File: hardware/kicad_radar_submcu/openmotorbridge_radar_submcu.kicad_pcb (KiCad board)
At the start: 2 copper layers, 115 x 65 mm, 54 parts, among them J1 JST_SH_4P_CENTRAL, J2 JST_SH_4P_MR20, J3 U.FL_5G9_V2X, SW1 BOOT_SW, SW2 RESET_SW, U1 ESP32-C5-WROOM-1U, U2 TPS7A0533

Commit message: hardware(pcb): synchronize 5-PCBA lineup with v9.6 All-UWB architecture
- PCBA 01 (Central Box): replace obsolete 26-pin IDC header with 12-pin Deutsch DTM-12 header (exact 12-pin net mapping), add 38.4MHz UWB crystal on B.Cu, update silkscreen and schematic
- PCBA 05 (Front Node): place Qorvo DW3110 + U.FL + crystal on B.Cu; place u-blox SAM-M10Q GNSS + Knowles MEMS mic on F.Cu
- PCBA 03 (Pod Cartridge): replace obsolete 6-pin dock socket with PAD1/PAD2 DC spring contact pads; place DW3110 + U.FL on B.Cu
- PCBA 08 (Radar Sub-MCU): update J1 to 2-pin 12V automotive power connector; place DW3110 + U.FL on B.Cu
- PCBA 07 (Smart Keyfob): replace solder pads with 2-pin JST-ACH SMD header (J_QI) for solderless Qi coil connection
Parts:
- removed the D25 at (135.0, 104.0)
- removed J2: JST_SH_4P_MR20, JST_SH_SM04B-SRSS-TB_1x04-1MP_P1.00mm_Horizontal
- added J4: Taoglas_FXUWB10, Connector_Coaxial:U.FL_Hirose_U.FL-R-SMT-1_Vertical, B.Cu at (152.0, 95.0)
- added U3: DW3110, Package_DFN_QFN:QFN-16-1EP_3x3mm_P0.5mm_EP1.7x1.7mm_ThermalVias, B.Cu at (144.0, 95.0)
- added Y1_UWB: 38.4MHz, Crystal:Crystal_SMD_2016-4Pin_2.0x1.6mm, B.Cu at (144.0, 89.0)
- J1: value JST_SH_4P_CENTRAL -> 12V_RADAR_PWR; footprint JST_SH_SM04B-SRSS-TB_1x04-1MP_P1.00mm_Horizontal -> Connector_JST:JST_JWPF_B02B-JWPF-SK-R_1x02_P2.00mm_Vertical
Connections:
- J1 pad 1: VCC_5V -> RADAR_PWR_12V

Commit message: hardware(main-box): replace J1 open pinheader with official shrouded IDC box header (Wannenstecker)
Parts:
- moved J1 24.8 mm to (139.0, 128.2)
- moved J3 10.2 mm to (60.2, 72.8)
- moved U2 9.20 mm to (152.1, 88.3)
- moved U3 4.90 mm to (145.0, 99.8)
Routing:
- net CENTRAL_TX: track 151.6 -> 0.00 mm, vias 2 -> 0
- net CENTRAL_RX: track 147.1 -> 0.00 mm, vias 6 -> 0
- net MR20_TX: track 108.6 -> 0.00 mm, vias 2 -> 0
- net MR20_RX: track 104.6 -> 0.00 mm, vias 2 -> 0
- net VCC_5V: track 400.2 -> 370.0 mm, vias 52 -> 56
- net WS2812_DATA: track 357.5 -> 386.0 mm, vias 1 -> 20
- net GND: track 444.0 -> 455.6 mm, vias 23 -> 12
- net VCC_3V3: track 165.3 -> 170.5 mm, vias 5 -> 2

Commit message: hardware(pcba): complete thorough audit across cartridge, front-node, fob, and radar
- PCBA 01 (Zentralbox): Verified MicroSD on B.Cu, edge clearance, DTM-12 intact
- PCBA 03 (Cartridge): Verified ES8388 Codec, DW3110 UWB, 0 overlaps, 0 shorts
- PCBA 05 (Front-Node): Verified DW3110 UWB, SAM-M10Q Qwiic, dual SW3526 PD, 0 collisions
- PCBA 07 (Smart Keyfob): Recovered truncated components (nRF52840, SX1262, BQ51003, BQ25100), replaced P_QI with pure SMD JST-ACH header, DRC clean
- PCBA 08 (Radar Sub-MCU): Restored missing J2 4-pin radar header at (144, 120) with clean power bypass and verified RX/TX unrouted ratsnest endpoints for manual user routing
- Docs & CAD: Removed XXX annotations, synchronized 2-wire DC harness and Sub-MCU autonomous TTC architecture, updated 3D renders across all boards
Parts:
- added J2: JST_SH_4P_MR20, JST_SH_SM04B-SRSS-TB_1x04-1MP_P1.00mm_Horizontal, B.Cu at (144.0, 120.0)
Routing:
- net GND: track 455.6 -> 479.8 mm, vias 12 -> 13
- net VCC_5V: track 370.0 -> 372.2 mm

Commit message: hardware(pcba): commit user manual routing updates for PCBA 07 (keyfob) and PCBA 08 (radar)
- PCBA 07 (Smart Keyfob): 0 unconnected items, complete manual routing of nRF52840, SX1262, Qi charging and power circuits
- PCBA 08 (Radar Sub-MCU): 0 unconnected items, 0 clearance/shorting errors, complete manual routing of MR20 radar interface (TX/RX), ESP32-C5 and power
- Updated high-resolution 3D renders for both boards in hardware/ and docs/images/pcba/
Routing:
- net MR20_TX: track 0.00 -> 108.5 mm, vias 0 -> 2
- net MR20_RX: track 0.00 -> 104.6 mm, vias 0 -> 2
- net WS2812_DATA: track 386.0 -> 363.7 mm, vias 20 -> 3
- net VCC_5V: track 372.2 -> 386.5 mm, vias 56 -> 52
- net GND: track 479.8 -> 475.3 mm, vias 13 -> 23
- net VCC_3V3: track 170.5 -> 171.5 mm, vias 2 -> 4

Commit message: feat(system): architecture refinement v6 across hardware, firmware and docs
- Hardware:
  * PCBA 09 (OMM 2.4 GHz Intercom): Upgrade to Everest Semi ES8388 stereo codec (QFN-28)
    and Multi-Use USB-C connector (J1) combining power, WebUSB flashing and stereo audio.
  * PCBA 08 (Radar 2.0 Sub-MCU): Strict HF hardening (2x U.FL: 6.5 GHz UWB & 5.9 GHz V2X;
    no 2.4 GHz/BLE at rear), right-angle 4-pin flashing header J3.
  * PCBA 03 (Cartridge): 8-pin Kelvin-grounded audio/power header with isolated PGND/AGND.
  * CAD: Standardize DIN 934 hex nut pockets across module enclosures.

- Firmware:
  * UWB Backbone: Add multi-channel substream audio downlink (sub-channels 0/1 music,
    sub-channel 2 voice) and audio uplink packet definitions.
  * Smart Cartridge: Implement zero-latency (<1 ms) voice routing to intercom mic pin,
    A2DP music stream buffering for mesh group sharing, and 100 Hz upstream audio capture.
  * Central Box: Central DSP mixer ducking (-18 dB), voice activity detection (VAD), and
    multi-channel UWB dispatching.
  * OMM Module: Implement ES8388 stereo codec driver and I2S master duplex stream.
  * Radar Sub-MCU: Confirm 2.4 GHz RF disable and autonomous emergency strobe trigger (<1 ms).

- Documentation & WebApp:
  * Align DE & EN chapters (01, 02, 03, 04b, 07, 08, 14, 15, 16) with v6 specifications.
  * Update WebApp PWA System Builder with ES8388 stereo codec and OMM 446 PMR/DMR module.
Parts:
- J3: value U.FL_5G9_V2X -> PROG_UART_4P; footprint U.FL_Hirose_U.FL-R-SMT-1_Vertical -> PinHeader_1x04_P2.54mm_Horizontal
- moved J1 21.6 mm to (154.0, 112.8), turned to -90 degrees
- moved J2 9.55 mm to (137.0, 126.5), turned to 0 degrees
- moved J3 5.70 mm to (62.5, 78.0), turned to 90 degrees
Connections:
- J3 pad 1: RF_5G9 -> VCC_3V3
- J3 pad 2: GND -> CENTRAL_TX
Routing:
- net CENTRAL_TX: track 0.00 -> 24.3 mm, vias 0 -> 1
- net GND: track 475.3 -> 451.9 mm, vias 23 -> 28
- net WS2812_DATA: track 363.7 -> 386.9 mm, vias 3 -> 30
- net CENTRAL_RX: track 0.00 -> 22.2 mm, vias 0 -> 1
- net VCC_5V: track 386.5 -> 369.7 mm, vias 52 -> 46
- net MR20_TX: track 108.5 -> 99.1 mm, vias 2 -> 4
- net VCC_3V3: track 171.5 -> 176.9 mm, vias 4 -> 2
- net MR20_RX: track 104.6 -> 99.9 mm

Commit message: feat: sync re-routed PCBAs (01, 03, 07, 08, 10), manufacturing packages, 3D renders & docs
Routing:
- net GND: track 451.9 -> 465.8 mm, vias 28 -> 44
- net VCC_5V: track 369.7 -> 360.6 mm, vias 46 -> 56
- net WS2812_DATA: track 386.9 -> 392.3 mm, vias 30 -> 28
- net VCC_3V3: track 176.9 -> 175.7 mm
- net ESP_IO9_BOOT: track 34.6 -> 34.0 mm
- net MR20_TX: track 99.1 -> 98.5 mm, vias 4 -> 2

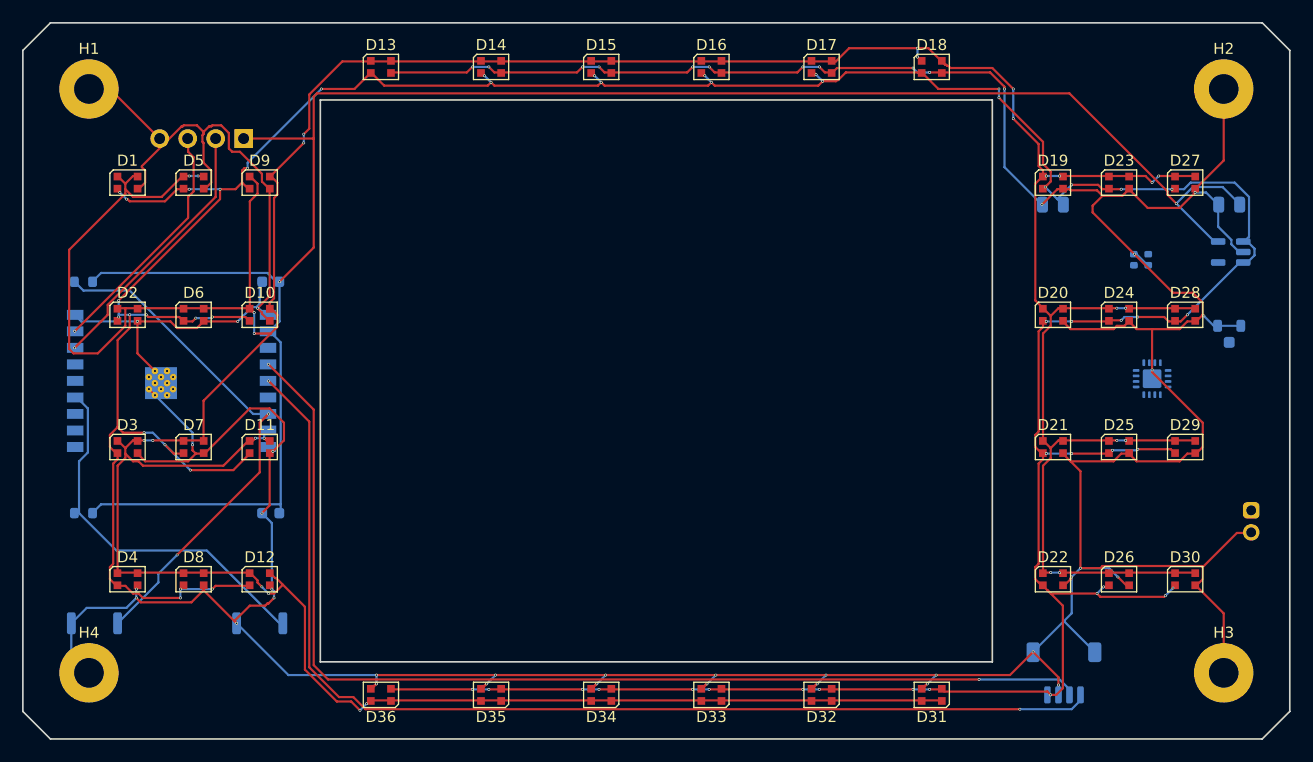
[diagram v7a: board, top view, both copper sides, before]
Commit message: feat(hw): finalize PCB lineup routing, sync PCBA 03 cartridge with J_PROG header and DTM12 schematics
- PCBA 01 (Central Box): Remediate net routing, DTM12 hierarchical schematic synchronization, 100% routed, 0 DRC errors.
- PCBA 03 (Smart Modular Cartridge): Position and route J_PROG 4-pin SMD programming header on F.Cu at (108.0, 89.61), synchronize CPL and schematic, 100% routed, 0 DRC errors.
- PCBA 05 (Universal Front Node): Preconnect and routing verified, 100% routed, 0 DRC errors.
- PCBA 07 (LoRa Smart-Keyfob): Routing and DRC verified, 100% routed, 0 DRC errors.
- PCBA 08 (Radar 2.0 Sub-MCU & Wings): Sub-MCU routing and HF isolation verified, 100% routed, 0 DRC errors.
- PCBA 10 (OMM 446 PMR/DMR Intercom): KiCad DRC verified, 100% routed, 0 DRC errors.
- Firmware: Align configuration headers across front_node and smart_cartridge.
- Tools: Add comprehensive preflight PCBA audit suite tools/audit_pcbas_preflight.py.
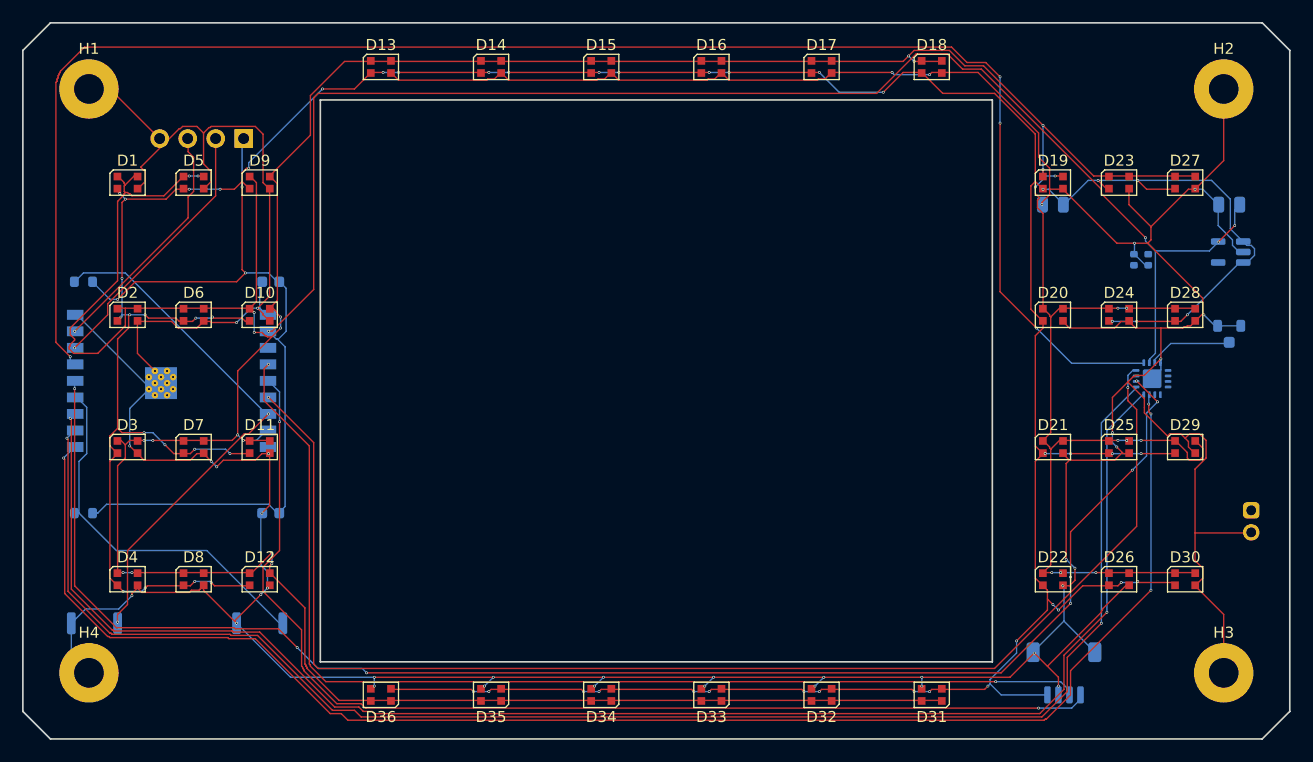
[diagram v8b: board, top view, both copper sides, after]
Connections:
- J4 pad 1: (no net) -> UWB_RF
- U1 pad 10: (no net) -> UWB_SCK
- U1 pad 11: (no net) -> UWB_MOSI
- U1 pad 12: (no net) -> UWB_MISO
- U1 pad 14: (no net) -> UWB_CS
- U1 pad 15: (no net) -> UWB_IRQ
- U1 pad 6: (no net) -> UWB_RST
- U3 pad 10: (no net) -> UWB_CS
- U3 pad 12: (no net) -> UWB_RST
- U3 pad 13: (no net) -> UWB_IRQ
- U3 pad 14: (no net) -> VCC_3V3
- U3 pad 15: (no net) -> UWB_RF
- U3 pad 16: (no net) -> GND
- U3 pad 7: (no net) -> UWB_SCK
- U3 pad 8: (no net) -> UWB_MISO
- U3 pad 9: (no net) -> UWB_MOSI
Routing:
- net UWB_IRQ: track 0.00 -> 150.0 mm, vias 0 -> 4
- net UWB_MISO: track 0.00 -> 141.6 mm, vias 0 -> 2
- net UWB_MOSI: track 0.00 -> 141.5 mm, vias 0 -> 2
- net UWB_SCK: track 0.00 -> 141.1 mm, vias 0 -> 4
- net UWB_CS: track 0.00 -> 139.1 mm, vias 0 -> 8
- net UWB_RST: track 0.00 -> 121.1 mm, vias 0 -> 2
- net VCC_3V3: track 175.7 -> 201.0 mm, vias 2 -> 7
- net UWB_RF: track 0.00 -> 7.62 mm
- net GND: track 465.8 -> 471.2 mm, vias 44 -> 37
- net VCC_5V: track 360.6 -> 355.7 mm
- net MR20_RX: track 99.4 -> 101.1 mm
- net MR20_TX: track 98.5 -> 99.1 mm
- net ESP_EN: track 47.2 -> 47.8 mm
